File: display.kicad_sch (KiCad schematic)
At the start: 24 parts, among them J701 Socket_Molex_SlimStack_2x20_5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, J702 HDMI-A_WE_685119134923

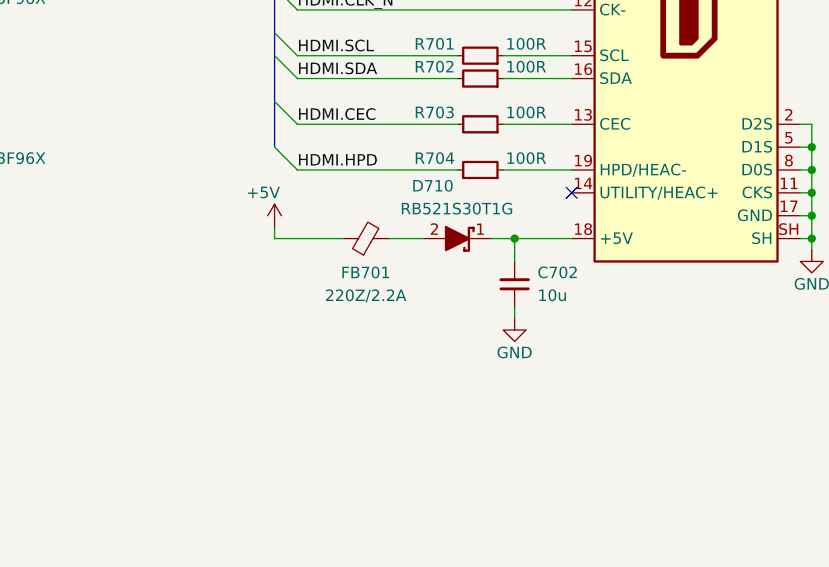
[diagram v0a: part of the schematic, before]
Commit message: [#55247] Change USB schematic: Remove PD from App USB, add CC controller
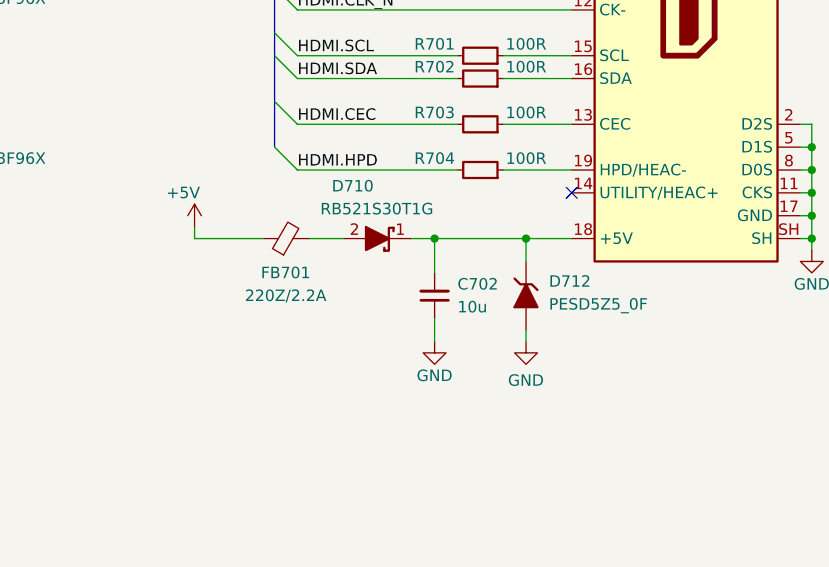
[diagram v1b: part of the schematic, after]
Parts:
- added D712: PESD5Z5_0F, antmicro-footprints:SOD-523, symbol antmicroTVSDiodes:PESD5Z5_0F
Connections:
- net GND: now also D712.2
- net at C702.2, D710.1, J702.18 (+5V): now also D712.1
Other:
- moved on the sheet: C702, D710, FB701

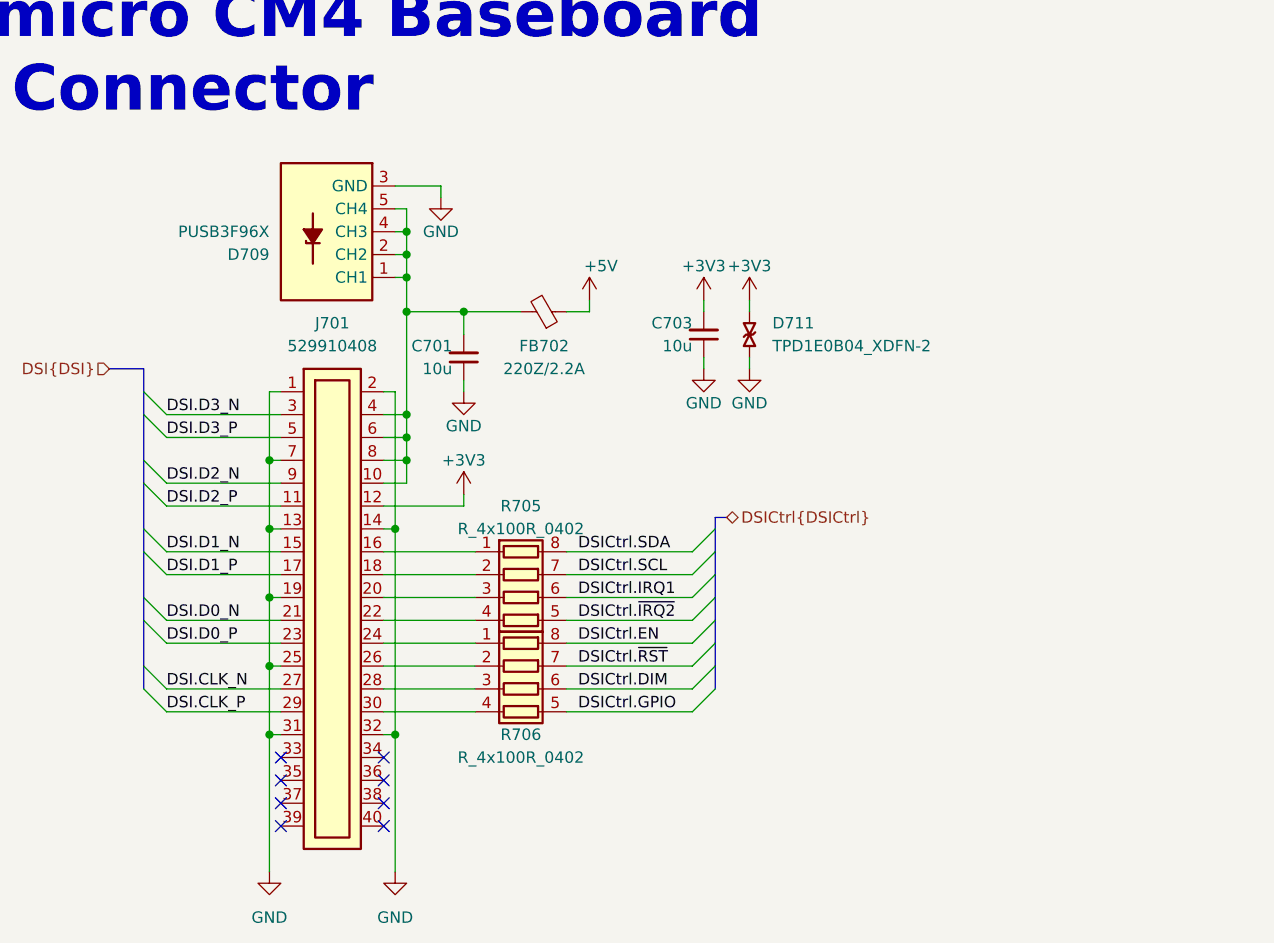
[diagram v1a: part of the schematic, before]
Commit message: [#55181] PCB: HDMI & adapter conn. placement
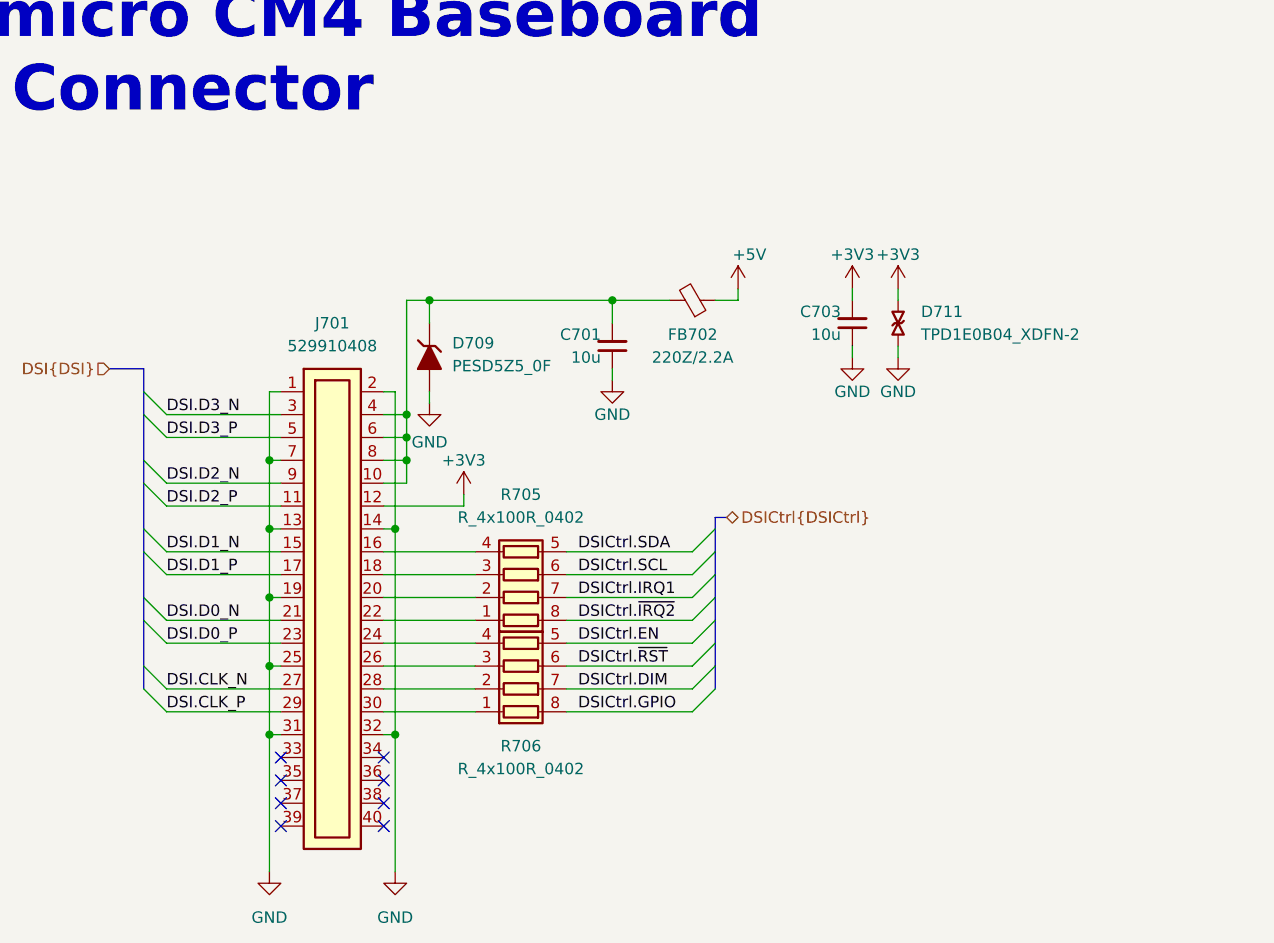
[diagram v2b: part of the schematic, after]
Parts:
- removed D709: PUSB3F96X_PASS, antmicro-footprints:Nexperia_DFN-10_2.5x1mm_P0.5mm, symbol antmicroTVSDiodes:PUSB3F96X_PASS
- added D709: PESD5Z5_0F, antmicro-footprints:SOD-523, symbol antmicroTVSDiodes:PESD5Z5_0F
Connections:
- net DSICtrl.DIM: now also R706.7 (R2.2); no longer R706.6 (R3.2)
- net DSICtrl.EN: now also R706.5 (R4.2); no longer R706.8 (R1.2)
- net DSICtrl.GPIO: now also R706.8 (R1.2); no longer R706.5 (R4.2)
- net DSICtrl.IRQ1: now also R705.7 (R2.2); no longer R705.6 (R3.2)
- net DSICtrl.SCL: now also R705.6 (R3.2); no longer R705.7 (R2.2)
- net DSICtrl.SDA: now also R705.5 (R4.2); no longer R705.8 (R1.2)
- net DSICtrl.~{IRQ2}: now also R705.8 (R1.2); no longer R705.5 (R4.2)
- net DSICtrl.~{RST}: now also R706.6 (R3.2); no longer R706.7 (R2.2)
- net GND: now also D709.2
- net at C701.2, FB702.2, J701.10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: now also D709.1
- net at J701.16: now also R705.4 (R4.1); no longer R705.1 (R1.1)
- net at J701.18: now also R705.3 (R3.1); no longer R705.2 (R2.1)
- net at J701.20: now also R705.2 (R2.1); no longer R705.3 (R3.1)
- net at J701.22: now also R705.1 (R1.1); no longer R705.4 (R4.1)
- net at J701.24: now also R706.4 (R4.1); no longer R706.1 (R1.1)
- net at J701.26: now also R706.3 (R3.1); no longer R706.2 (R2.1)
- net at J701.28: now also R706.2 (R2.1); no longer R706.3 (R3.1)
- net at J701.30: now also R706.1 (R1.1); no longer R706.4 (R4.1)
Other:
- moved on the sheet: C701, C703, D711, FB702

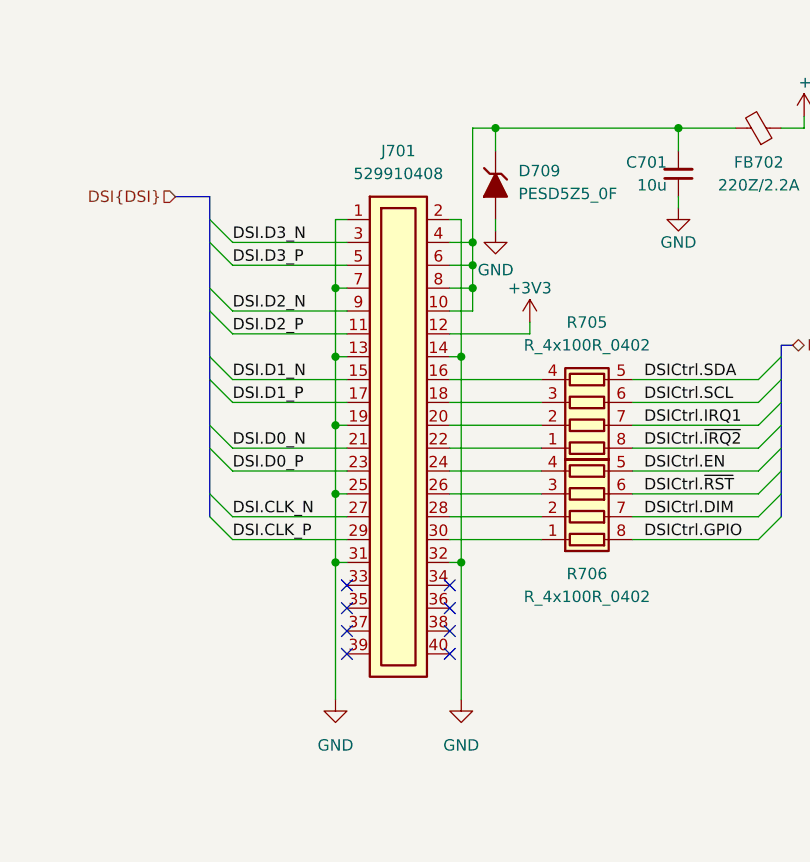
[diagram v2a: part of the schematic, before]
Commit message: [#55181] Placement: SD& GPIO; Change adapter conn. back to H2mm; flip adapter stub
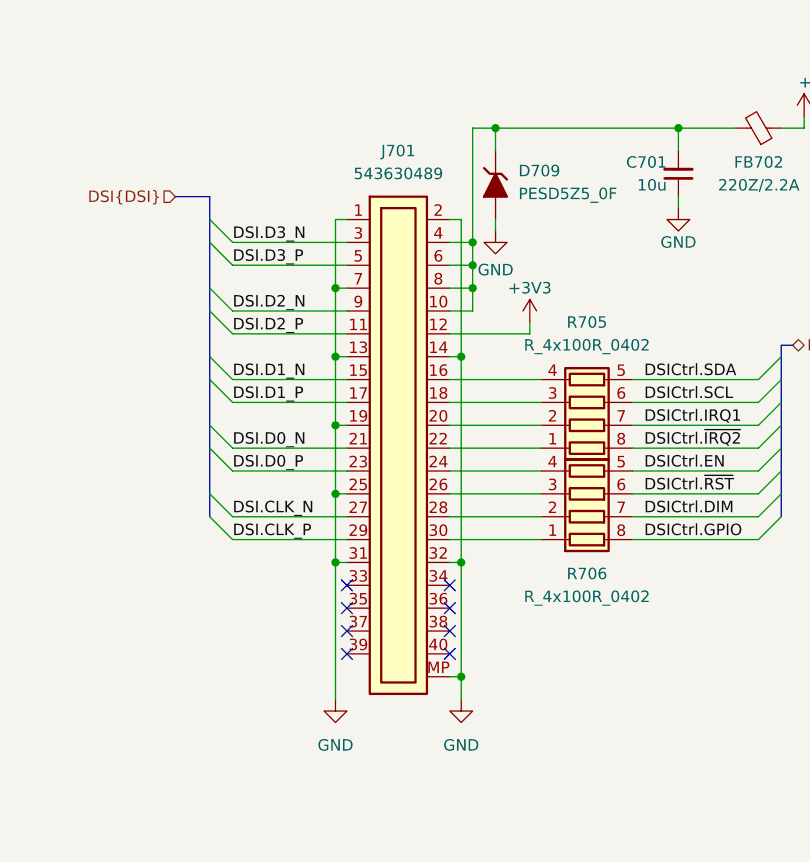
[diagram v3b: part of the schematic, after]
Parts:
- J701: footprint antmicro-footprints:Conn_Socket_Molex_SlimStack_2x20_529910408 -> antmicro-footprints:Conn_Socket_Molex_SlimStack_2x20_543630489; symbol antmicroB2BConnectors:Socket_Molex_SlimStack_2x20_529910408 -> antmicroB2BConnectors:Socket_Molex_SlimStack_2x20_543630489; MPN 529910408 -> 543630489
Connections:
- net GND: now also J701.MP
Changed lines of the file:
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@@
   (junction (at 287.02 83.82) (diameter 0) (color 0 0 0 0)
   )
+  (junction (at 234.95 233.68) (diameter 0) (color 0 0 0 0)
+  )
   (junction (at 287.02 91.44) (diameter 0) (color 0 0 0 0)
   )
@@
     (stroke (width 0) (type default))
   )
+  (wire (pts (xy 233.68 233.68) (xy 234.95 233.68))
+    (stroke (width 0) (type default))
+  )
   (bus (pts (xy 270.51 196.85) (xy 270.51 198.12))
     (stroke (width 0) (type default))
@@
     (stroke (width 0) (type default))
   )
-  (wire (pts (xy 234.95 220.98) (xy 234.95 236.22))
+  (wire (pts (xy 234.95 220.98) (xy 234.95 233.68))
     (stroke (width 0) (type default))
   )
@@
     (stroke (width 0) (type default))
   )
+  (wire (pts (xy 234.95 233.68) (xy 234.95 236.22))
+    (stroke (width 0) (type default))
+  )
   (wire (pts (xy 233.68 182.88) (xy 234.95 182.88))
     (stroke (width 0) (type default))
@@
     (effects (font (size 1.27 1.27)) (justify left))
   )
-  (symbol (lib_id "antmicroB2BConnectors:Socket_Molex_SlimStack_2x20_529910408") (at 222.25 182.88 0) (unit 1)
+  (symbol (lib_id "antmicroB2BConnectors:Socket_Molex_SlimStack_2x20_543630489") (at 222.25 182.88 0) (unit 1)
     (in_bom yes) (on_board yes) (dnp no) (fields_autoplaced)
     (property "Reference" "J701" (at 227.965 175.26 0)
@@
       (effects (font (size 1.27 1.27) (thickness 0.15)) (justify left bottom) hide)
     )
-    (property "Footprint" "antmicro-footprints:Conn_Socket_Molex_SlimStack_2x20_529910408" (at 247.65 190.5 0)
+    (property "Footprint" "antmicro-footprints:Conn_Socket_Molex_SlimStack_2x20_543630489" (at 247.65 190.5 0)
       (effects (font (size 1.27 1.27) (thickness 0.15)) (justify left bottom) hide)
     )
-    (property "Datasheet" "https://www.molex.com/en-us/products/part-detail/529910408?display=pdf" (at 247.65 193.04 0)
+    (property "Datasheet" "https://www.molex.com/pdm_docs/sd/543630489_sd.pdf" (at 247.65 193.04 0)
       (effects (font (size 1.27 1.27) (thickness 0.15)) (justify left bottom) hide)
     )
-    (property "MPN" "529910408" (at 227.965 177.8 0)
+    (property "MPN" "543630489" (at 227.965 177.8 0)
       (effects (font (size 1.27 1.27) (thickness 0.15)))
     )
@@
     (pin "35")
     (pin "34")
+    (pin "MP")
     (instances
       (project "cm4-baseboard"

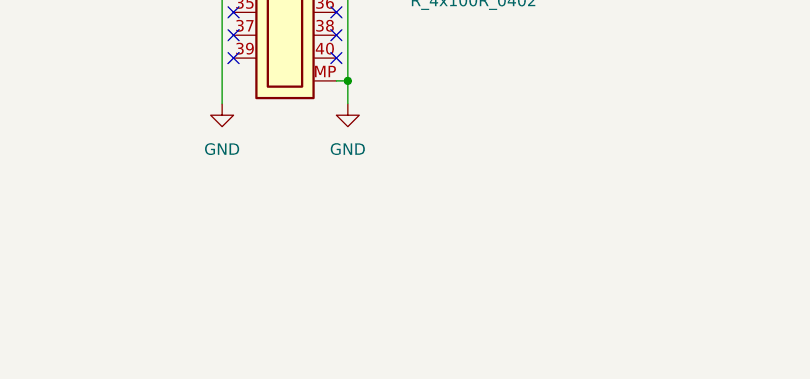
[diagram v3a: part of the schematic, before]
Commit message: [#55181] Change adapter spacer to 2mm; update spacers from lib
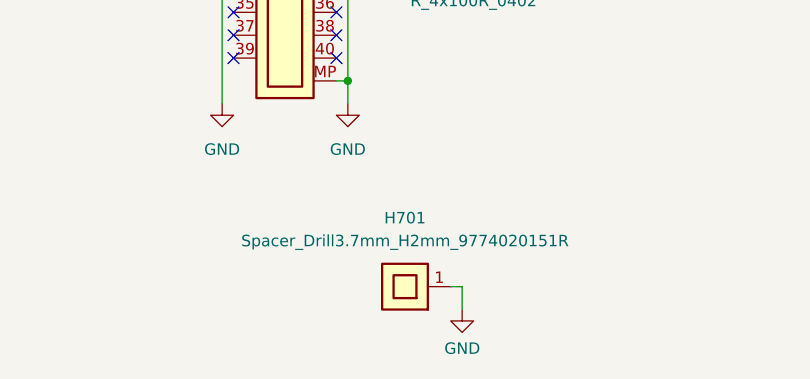
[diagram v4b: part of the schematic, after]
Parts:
- added H701: Spacer_Drill3.7mm_H2mm_9774020151R, antmicro-footprints:Spacer_Drill3.7mm_H2mm_9774020151R, symbol antmicroMechanicalParts:Spacer_Drill3.7mm_H2mm_9774020151R
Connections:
- net GND: now also H701.1
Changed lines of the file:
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@@
     (stroke (width 0) (type default))
   )
+  (wire (pts (xy 246.38 256.54) (xy 247.65 256.54))
+    (stroke (width 0) (type default))
+  )
   (bus (pts (xy 140.97 181.61) (xy 140.97 184.15))
     (stroke (width 0) (type default))
@@
     (stroke (width 0) (type default))
   )
+  (wire (pts (xy 247.65 256.54) (xy 247.65 259.08))
+    (stroke (width 0) (type default))
+  )
   (bus (pts (xy 140.97 162.56) (xy 140.97 165.1))
     (stroke (width 0) (type default))
@@
     )
   )
+  (symbol (lib_id "antmicropower:GND") (at 247.65 259.08 0) (mirror y) (unit 1)
+    (in_bom yes) (on_board yes) (dnp no) (fields_autoplaced)
+    (property "Reference" "#PWR0722" (at 238.76 261.62 0)
+      (effects (font (size 1.27 1.27) (thickness 0.15)) (justify left bottom) hide)
+    )
+    (property "Value" "GND" (at 249.6602 264.16 0)
+      (effects (font (size 1.27 1.27) (thickness 0.15)) (justify left bottom))
+    )
+    (property "Footprint" "" (at 238.76 266.7 0)
+      (effects (font (size 1.27 1.27) (thickness 0.15)) (justify left bottom) hide)
+    )
+    (property "Datasheet" "" (at 238.76 271.78 0)
+      (effects (font (size 1.27 1.27) (thickness 0.15)) (justify left bottom) hide)
+    )
+    (property "Author" "Antmicro" (at 238.76 266.7 0)
+      (effects (font (size 1.27 1.27) (thickness 0.15)) (justify left bottom) hide)
+    )
+    (property "License" "Apache-2.0" (at 238.76 269.24 0)
+      (effects (font (size 1.27 1.27) (thickness 0.15)) (justify left bottom) hide)
+    )
+    (pin "1")
+    (instances
+      (project "cm4-baseboard"
+        (path "/60b842dc-0853-4a25-99ac-5784ddf94d0d/b148dc70-7270-4ae3-80a1-580624d4cd31"
+          (reference "#PWR0722") (unit 1)
+        )
+      )
+    )
+  )
   (symbol (lib_id "antmicropower:+5V") (at 273.05 171.45 0) (mirror y) (unit 1)
     (in_bom yes) (on_board yes) (dnp no)
@@
         )
       )
+    )
+  )
+  (symbol (lib_id "antmicroMechanicalParts:Spacer_Drill3.7mm_H2mm_9774020151R") (at 246.38 256.54 0) (mirror y) (unit 1)
+    (in_bom yes) (on_board yes) (dnp no) (fields_autoplaced)
+    (property "Reference" "H701" (at 241.3 248.92 0)
+      (effects (font (size 1.27 1.27) (thickness 0.15)))
+    )
+    (property "Value" "Spacer_Drill3.7mm_H2mm_9774020151R" (at 241.3 251.46 0)
+      (effects (font (size 1.27 1.27) (thickness 0.15)))
+    )
+    (property "Footprint" "antmicro-footprints:Spacer_Drill3.7mm_H2mm_9774020151R" (at 223.52 264.16 0)
+      (effects (font (size 1.27 1.27) (thickness 0.15)) (justify left bottom) hide)
+    )
+    (property "Datasheet" "https://www.we-online.com/components/products/datasheet/9774020151R.pdf" (at 223.52 266.7 0)
+      (effects (font (size 1.27 1.27) (thickness 0.15)) (justify left bottom) hide)
+    )
+    (property "Manufacturer" "Würth Elektronik" (at 223.52 269.24 0)
+      (effects (font (size 1.27 1.27) (thickness 0.15)) (justify left bottom) hide)
+    )
+    (property "MPN" "9774020151R" (at 223.52 271.78 0)
+      (effects (font (size 1.27 1.27) (thickness 0.15)) (justify left bottom) hide)
+    )
+    (property "Author" "Antmicro" (at 223.52 274.32 0)
+      (effects (font (size 1.27 1.27) (thickness 0.15)) (justify left bottom) hide)
+    )
+    (property "License" "Apache-2.0" (at 223.52 276.86 0)
+      (effects (font (size 1.27 1.27) (thickness 0.15)) (justify left bottom) hide)
+    )
+    (pin "1")
+    (instances
+      (project "cm4-baseboard"
+        (path "/60b842dc-0853-4a25-99ac-5784ddf94d0d/b148dc70-7270-4ae3-80a1-580624d4cd31"
+          (reference "H701") (unit 1)
+        )
+      )

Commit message: [#55532] Sch: Optimize conections for easier routing
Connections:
- net DSICtrl.DIM: now also R706.6 (R3.2); no longer R706.7 (R2.2)
- net DSICtrl.EN: now also R706.8 (R1.2); no longer R706.5 (R4.2)
- net DSICtrl.GPIO: now also R706.5 (R4.2); no longer R706.8 (R1.2)
- net DSICtrl.IRQ1: now also R705.6 (R3.2); no longer R705.7 (R2.2)
- net DSICtrl.~{IRQ2}: now also R705.5 (R4.2); no longer R705.8 (R1.2)
- net DSICtrl.~{RST}: now also R706.7 (R2.2); no longer R706.6 (R3.2)
- net at J701.16: now also R705.1 (R1.1); no longer R705.4 (R4.1)
- net at J701.18: now also R705.2 (R2.1); no longer R705.3 (R3.1)
- net at J701.20: now also R705.3 (R3.1); no longer R705.2 (R2.1)
- net at J701.22: now also R705.4 (R4.1); no longer R705.1 (R1.1)
- net at J701.24: now also R706.1 (R1.1); no longer R706.4 (R4.1)
- net at J701.26: now also R706.2 (R2.1); no longer R706.3 (R3.1)
- net at J701.28: now also R706.3 (R3.1); no longer R706.2 (R2.1)
- net at J701.30: now also R706.4 (R4.1); no longer R706.1 (R1.1)
- net DSICtrl.SCL renamed I_{2}C1.SCL
- net I_{2}C1.SCL: now also R705.7 (R2.2); no longer R705.6 (R3.2)
- net DSICtrl.SDA renamed I_{2}C1.SDA
- net I_{2}C1.SDA: now also R705.8 (R1.2); no longer R705.5 (R4.2)
